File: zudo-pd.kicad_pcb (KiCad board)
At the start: 2 copper layers, 82 x 99 mm, 84 parts, among them J1 USB-C, J10 2541WR-2X08P, J11 2541WR-2X08P, J6 1217754-1, J7 1217754-1, J8 1217754-1, J9 1217754-1, Q1 -30V -4A, U1 STUSB4500QTR, U2 LM2596S-ADJ, U3 LM2596S-ADJ, U4 LM2596S-ADJ, U6 L7812CD2T-TR, U7 L7805ABD2T-TR, U8 CJ7912_C94173

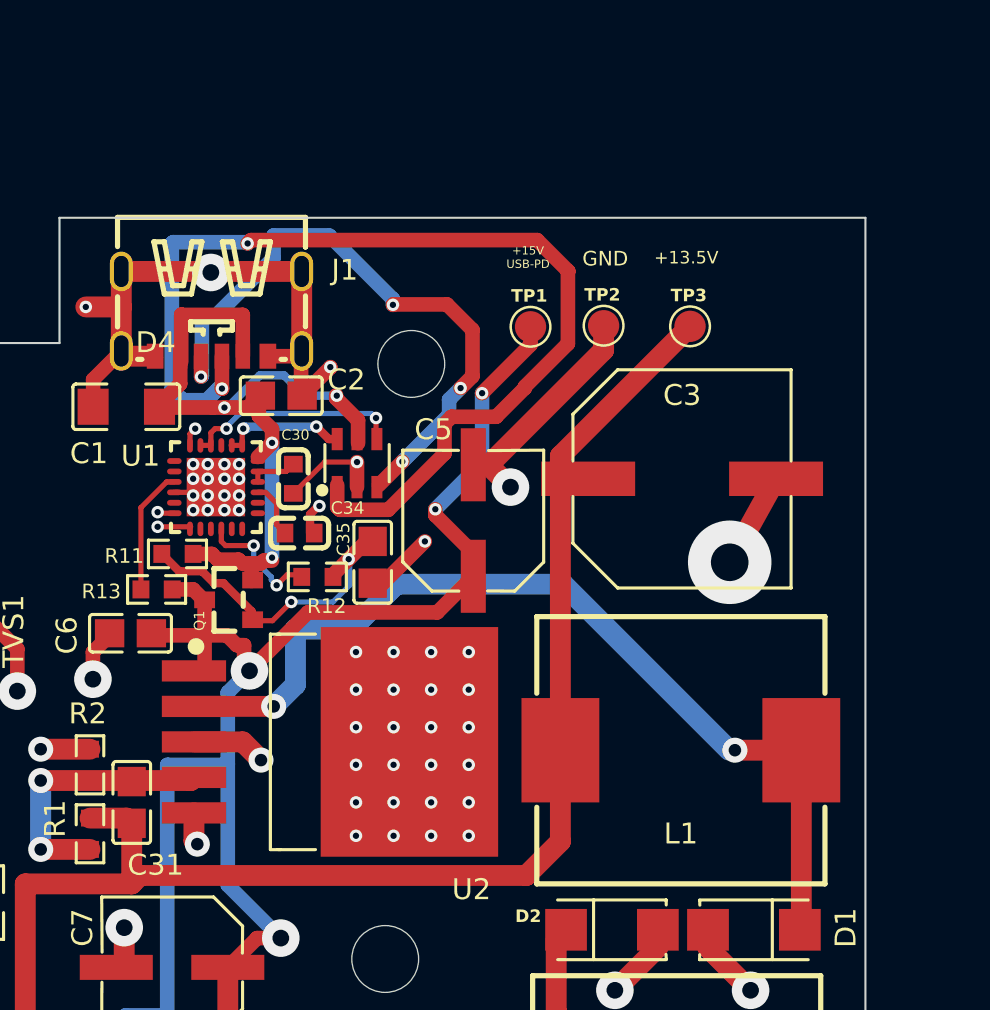
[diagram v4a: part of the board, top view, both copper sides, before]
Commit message: feat: Update KiCad project settings and PCB layout
Updated project configuration and PCB layout.

Co-Authored-By: Claude <noreply@anthropic.com>
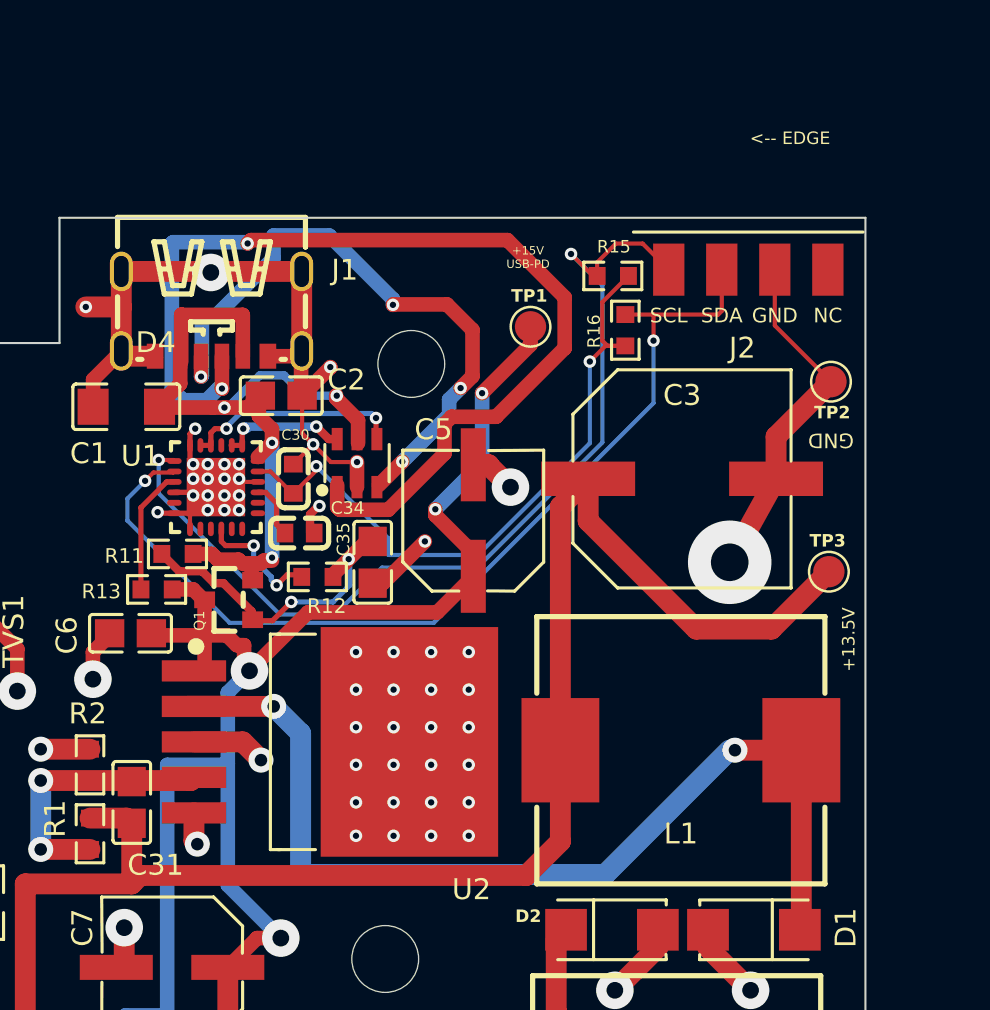
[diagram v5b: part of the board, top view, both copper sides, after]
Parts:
- added J2: Pogo pads, zudo-pd:PogoPad_1x04_P2.54mm, F.Cu at (70.4, 2.48)
- added R15: 4.7k, zudo-pd:R0603, F.Cu at (63.9, 2.79)
- added R16: 4.7k, zudo-pd:R0603, F.Cu at (64.5, 5.38)
- moved TP3 13.5 mm to (74.2, 16.9)
- moved TP2 11.2 mm to (74.3, 7.85), turned to 180 degrees
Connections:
- net +15V -> +13.5V gen renamed VBUS_OUT
- C1 pad 1: GND rail -> GND
- C11 pad 1: GND rail -> GND
- C14 pad 2: GND rail -> GND
- C15 pad 2: GND rail -> GND
- C17 pad 1: GND rail -> GND
- C18 pad 2: GND rail -> GND
- C2 pad 1: GND rail -> GND
- C20 pad 2: GND rail -> GND
- C21 pad 2: GND rail -> GND
- C22 pad 2: GND rail -> GND
- C23 pad 2: GND rail -> GND
- C3 pad 2: GND rail -> GND
- C30 pad 1: Net-(U1-VREG_2V7) -> GND
- C30 pad 2: GND rail -> VREG_2V7
- C33 pad 1: GND rail -> GND
- C34 pad 2: GND rail -> GND
- C35 pad 2: GND rail -> GND
- C4 pad 2: GND rail -> GND
- C5 pad 2: GND rail -> GND
- C6 pad 2: GND rail -> GND
- C7 pad 2: GND rail -> GND
- C8 pad 2: GND rail -> GND
- D1 pad 2: GND rail -> GND
- D2 pad 2: GND rail -> GND
- D4 pad 2: GND rail -> GND
- J1 pad 7: GND rail -> GND
- J1 pad A12: GND rail -> GND
- J1 pad B12: GND rail -> GND
- J10 pad 10: GND rail -> GND
- J10 pad 11: GND rail -> GND
- J10 pad 12: GND rail -> GND
- J10 pad 13: GND rail -> GND
- J10 pad 14: GND rail -> GND
- J10 pad 9: GND rail -> GND
- J11 pad 10: GND rail -> GND
- J11 pad 11: GND rail -> GND
- J11 pad 12: GND rail -> GND
- J11 pad 13: GND rail -> GND
- J11 pad 14: GND rail -> GND
- J11 pad 9: GND rail -> GND
- J9 pad 1: GND rail -> GND
- J9 pad 2: GND rail -> GND
- L3 pad 2: GND rail -> GND
- LED2 pad 1: GND rail -> GND
- LED3 pad 1: GND rail -> GND
- LED4 pad 2: GND rail -> GND
- R2 pad 1: GND rail -> GND
- R4 pad 2: GND rail -> GND
- R5 pad 2: GND rail -> GND
- TP2 pad 1: GND rail -> GND
- TVS1 pad 2: GND rail -> GND
- TVS2 pad 1: GND rail -> GND
- TVS3 pad 1: GND rail -> GND
- U1 pad 10: GND rail -> GND
- U1 pad 12: GND rail -> GND
- U1 pad 13: GND rail -> GND
- U1 pad 22: Net-(U1-VREG_2V7) -> GND
- U1 pad 23: Net-(U1-VREG_2V7) -> VREG_2V7
- U1 pad 25: GND rail -> GND
- U1 pad 6: GND rail -> GND
- U1 pad 7: unconnected-(U1-SCL-Pad7) -> SCL-pin1
- U1 pad 8: unconnected-(U1-SDA-Pad8) -> SDA-pin2
- U2 pad 3: GND rail -> GND
- U2 pad 5: GND rail -> GND
- U2 pad 6: GND rail -> GND
- U3 pad 3: GND rail -> GND
- U3 pad 5: GND rail -> GND
- U3 pad 6: GND rail -> GND
- U6 pad 4: GND rail -> GND
- U7 pad 2: GND rail -> GND
- U8 pad 1: GND rail -> GND
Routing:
- net GND: track 0.00 -> 189.3 mm, vias 0 -> 153
- net GND rail: track 181.2 -> 0.00 mm, vias 154 -> 0
- net SDA-pin2: track 0.00 -> 46.6 mm, vias 0 -> 2
- net SCL-pin1: track 0.00 -> 45.7 mm, vias 0 -> 2
- net VREG_2V7: track 0.00 -> 32.2 mm, vias 0 -> 2
- net /DC-DC Conversion/+13.5V OUT: track 94.4 -> 102.0 mm
- net Net-(D1-K): track 45.1 -> 47.5 mm
- net Net-(U1-VREG_2V7): track 2.29 -> 0.00 mm
- net Net-(J1-CC1): track 50.9 -> 49.9 mm
- added copper zone on B.Cu, net GND
- removed copper zone on B.Cu, net GND rail

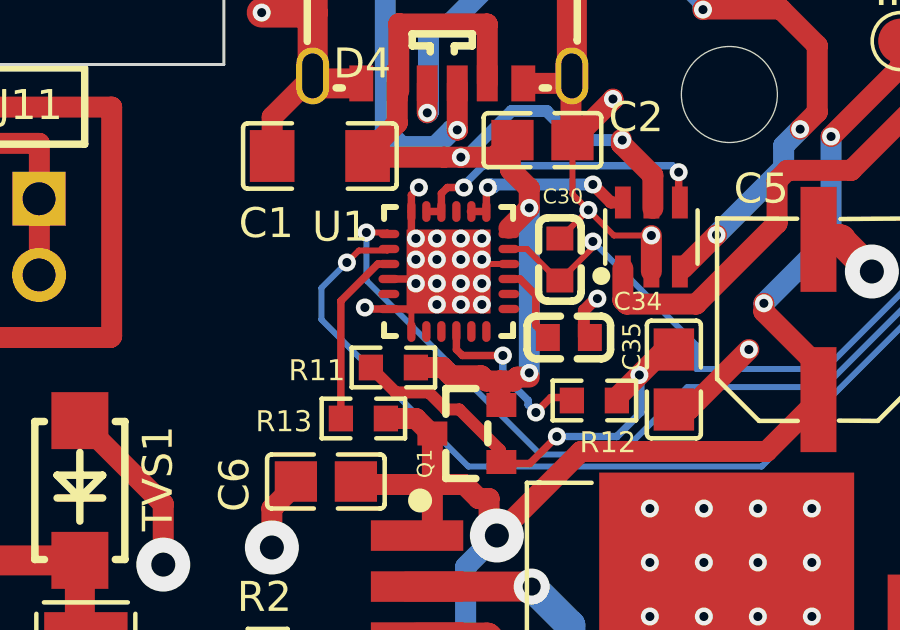
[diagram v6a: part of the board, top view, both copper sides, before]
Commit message: feat(hardware): v3 CC pin fix — external 10k Rd on CC1/CC2, CC1DB/CC2DB to GND
Fixed STUSB4500 USB-PD controller issue on v2 PCBAs where CC1DB was internally shorted to GND. Solution: added external 10kΩ pulldown resistors (R17/R18) on CC1/CC2 lines and rerouted U1 pins 1 (CC1DB) and 5 (CC2DB) directly to GND instead of CC1/CC2 nets. Updated BOM with all pulldown entries (R15/R16 existing, R17/R18 new for v3).

Co-Authored-By: Claude <noreply@anthropic.com>
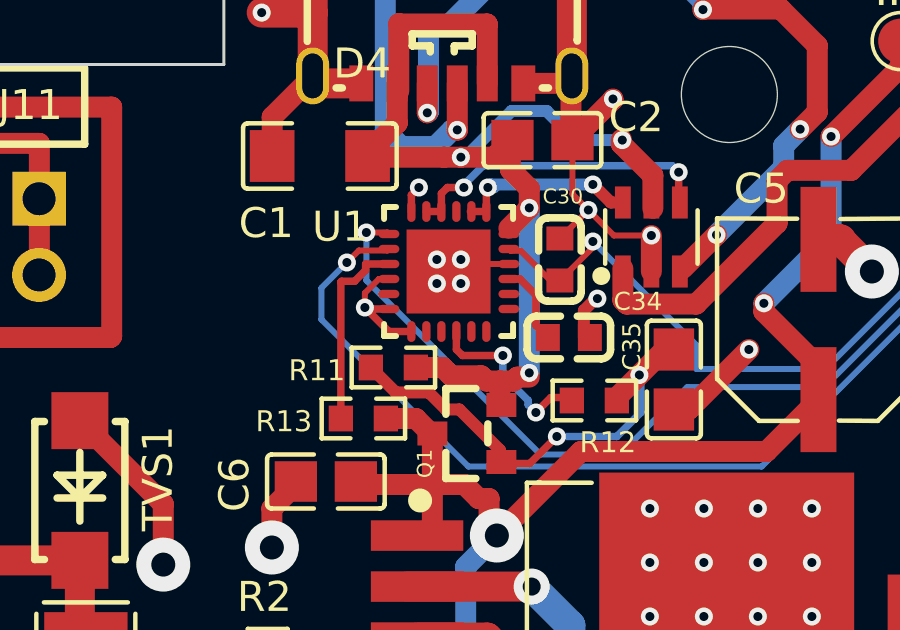
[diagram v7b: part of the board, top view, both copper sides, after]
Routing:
- net GND: track 189.3 -> 190.9 mm, vias 153 -> 142

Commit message: fix(pcb): adjust v3 pogo pad diameter (0.6mm → 0.5mm) and place R18 5.1k Rd resistor
Fine-tune pogo pad diameter for v3 test point block (J3) and place the external 5.1k Rd resistor
in USB-PD input stage, matching the schematic update from commit 68b4e18.

Co-Authored-By: Claude <noreply@anthropic.com>
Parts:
- added J3: Pogo pads (debug), zudo-pd:PogoPad_1x08_P2.54mm, F.Cu at (65.2, 97.2)
- added R17: 5.1k, zudo-pd:R0603, F.Cu at (55.8, 2.60)
- added R18: 5.1k, zudo-pd:R0603, F.Cu at (52.5, 2.55)
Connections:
- net Net-(U1-VBUS_EN_SNK) renamed VBEN
- U1 pad 1: Net-(U1-CC1) -> GND
- U1 pad 11: unconnected-(U1-ATTACH-Pad11) -> ATT
- U1 pad 20: unconnected-(U1-POWER_OK2-Pad20) -> PDOK
- U1 pad 5: Net-(U1-CC2) -> GND
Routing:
- net ATT: track 0.00 -> 124.4 mm, vias 0 -> 4
- net PDOK: track 0.00 -> 123.3 mm, vias 0 -> 2
- net VBEN: track 6.00 -> 118.3 mm, vias 2 -> 3
- net VBUS_IN: track 37.4 -> 149.4 mm, vias 4 -> 6
- net VREG_2V7: track 32.2 -> 130.6 mm, vias 2 -> 4
- net GND: track 190.9 -> 271.6 mm, vias 142 -> 145
- net VBUS_OUT: track 117.2 -> 119.3 mm
- net Net-(J1-CC2): track 30.4 -> 32.1 mm
- net SDA-pin2: track 46.6 -> 48.0 mm
- net Net-(J1-CC1): track 49.9 -> 50.7 mm
- net Net-(Q1-G): track 15.2 -> 15.8 mm
- net Net-(U1-CC2): track 10.8 -> 10.3 mm
- net Net-(U1-CC1): track 6.59 -> 6.09 mm
